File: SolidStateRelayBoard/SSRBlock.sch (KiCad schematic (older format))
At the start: 8 parts, among them Q201 MMBT2222ALT1G, U201 SSR

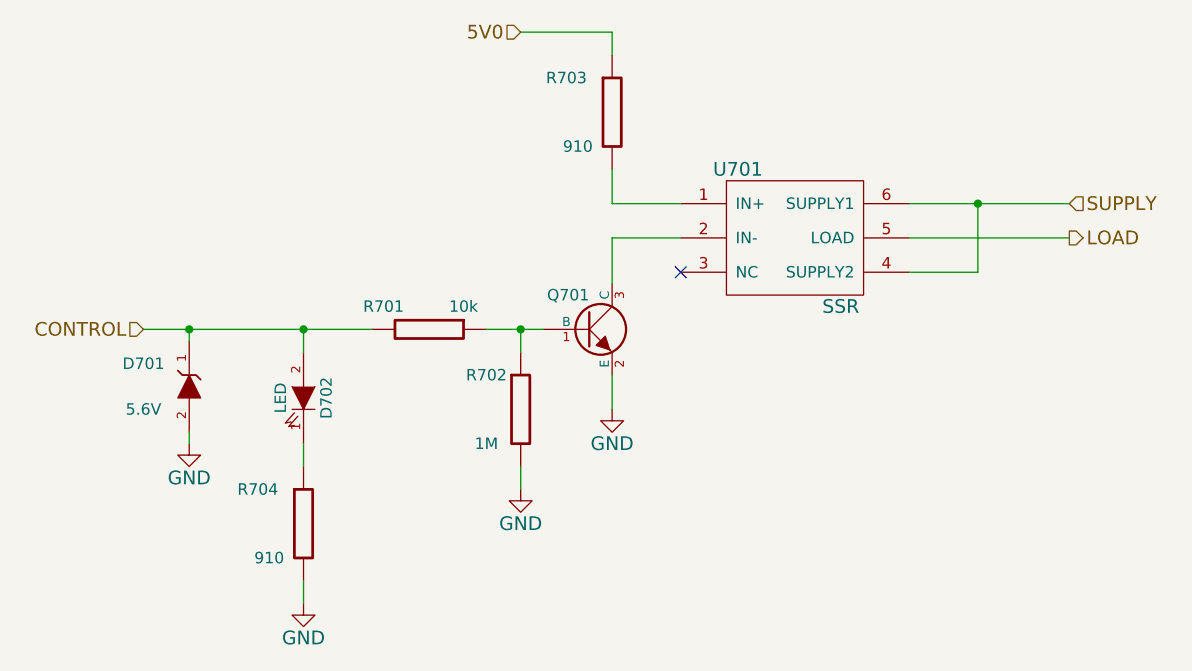
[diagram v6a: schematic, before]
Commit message: Big Changes to SSR
Made a footprint for the XTR and the transistor. Made XTR circuit and
made connected to that it will interface with the mpye’s
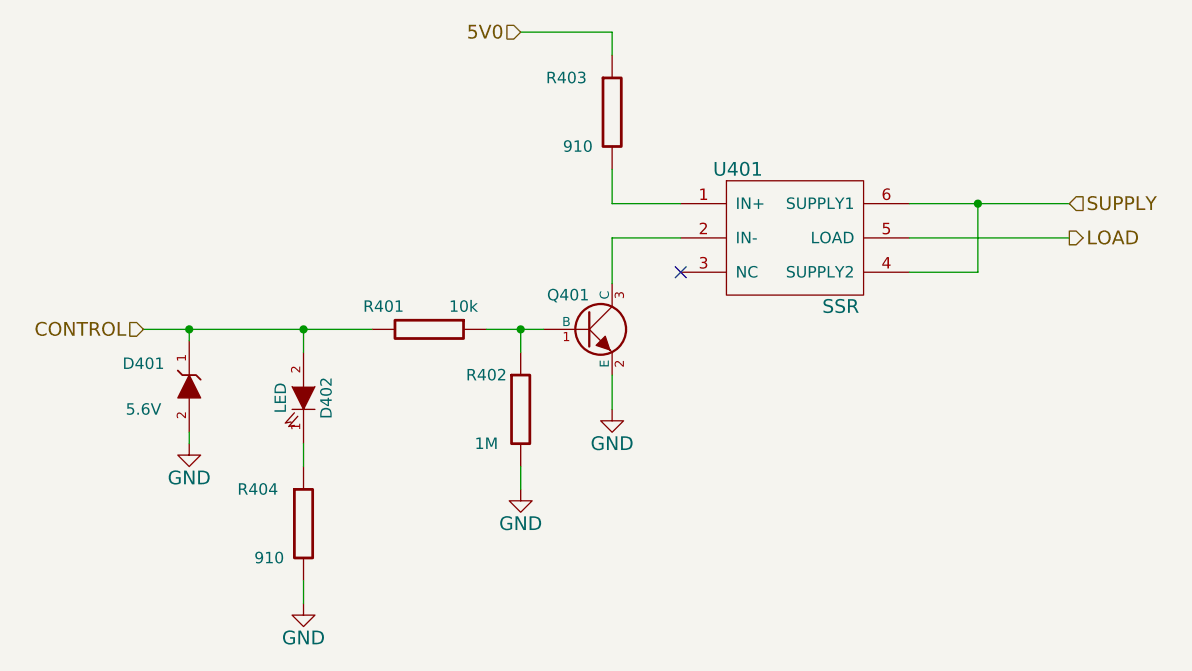
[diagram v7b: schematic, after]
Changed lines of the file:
@@
 $Descr A4 11693 8268
 encoding utf-8
-Sheet 7 14
+Sheet 4 14
 Title ""
 Date ""
@@
 AR Path="/586B7988/586B33BB" Ref="Q1601"  Part="1"
 AR Path="/586B7996/586B33BB" Ref="Q1701"  Part="1"
-F 0 "Q701" H 5100 3400 50  0000 R CNN
+F 0 "Q401" H 5100 3400 50  0000 R CNN
 F 1 "MMBT2222ALT1G" H 5100 3400 50  0001 R CNN
 F 2 "TO_SOT_Packages_SMD:SOT-23_Handsoldering" H 5100 3250 60  0001 C CNN
@@
 AR Path="/586B7988/586B33E9" Ref="R1603"  Part="1"
 AR Path="/586B7996/586B33E9" Ref="R1703"  Part="1"
-F 0 "R703" H 5000 2450 50  0000 C CNN
+F 0 "R403" H 5000 2450 50  0000 C CNN
 F 1 "910" H 5050 2150 50  0000 C CNN
 F 2 "Resistors_SMD:R_1206_HandSoldering" V 5130 2300 30  0001 C CNN
@@
 AR Path="/586B7988/586B3431" Ref="R1601"  Part="1"
 AR Path="/586B7996/586B3431" Ref="R1701"  Part="1"
-F 0 "R701" V 4300 3050 50  0000 C CNN
+F 0 "R401" V 4300 3050 50  0000 C CNN
 F 1 "10k" V 4300 3400 50  0000 C CNN
 F 2 "Resistors_SMD:R_1206_HandSoldering" V 4330 3250 30  0001 C CNN
@@
 	5200 3450 5200 3600
 $Comp
-L GND #PWR036
+L GND #PWR039
 U 1 1 586B354B
 P 5200 3600
-AR Path="/586B2B8E/586B354B" Ref="#PWR036"  Part="1"
-AR Path="/586B3F68/586B354B" Ref="#PWR040"  Part="1"
-AR Path="/586B4A2A/586B354B" Ref="#PWR044"  Part="1"
-AR Path="/586B4A38/586B354B" Ref="#PWR048"  Part="1"
-AR Path="/586B65A6/586B354B" Ref="#PWR052"  Part="1"
-AR Path="/586B65B4/586B354B" Ref="#PWR056"  Part="1"
-AR Path="/586B65C2/586B354B" Ref="#PWR060"  Part="1"
-AR Path="/586B65D0/586B354B" Ref="#PWR064"  Part="1"
-AR Path="/586B7934/586B354B" Ref="#PWR068"  Part="1"
-AR Path="/586B7942/586B354B" Ref="#PWR072"  Part="1"
-AR Path="/586B7950/586B354B" Ref="#PWR076"  Part="1"
-AR Path="/586B795E/586B354B" Ref="#PWR080"  Part="1"
-AR Path="/586B796C/586B354B" Ref="#PWR084"  Part="1"
+AR Path="/586B2B8E/586B354B" Ref="#PWR039"  Part="1"
+AR Path="/586B3F68/586B354B" Ref="#PWR043"  Part="1"
+AR Path="/586B4A2A/586B354B" Ref="#PWR047"  Part="1"
+AR Path="/586B4A38/586B354B" Ref="#PWR051"  Part="1"
+AR Path="/586B65A6/586B354B" Ref="#PWR055"  Part="1"
+AR Path="/586B65B4/586B354B" Ref="#PWR059"  Part="1"
+AR Path="/586B65C2/586B354B" Ref="#PWR063"  Part="1"
+AR Path="/586B65D0/586B354B" Ref="#PWR067"  Part="1"
+AR Path="/586B7934/586B354B" Ref="#PWR071"  Part="1"
+AR Path="/586B7942/586B354B" Ref="#PWR075"  Part="1"
+AR Path="/586B7950/586B354B" Ref="#PWR079"  Part="1"
+AR Path="/586B795E/586B354B" Ref="#PWR083"  Part="1"
+AR Path="/586B796C/586B354B" Ref="#PWR087"  Part="1"
 AR Path="/586B797A/586B354B" Ref="#PWR087"  Part="1"
 AR Path="/586B7988/586B354B" Ref="#PWR091"  Part="1"
 AR Path="/586B7996/586B354B" Ref="#PWR095"  Part="1"
-F 0 "#PWR056" H 5200 3350 60  0001 C CNN
+F 0 "#PWR087" H 5200 3350 60  0001 C CNN
 F 1 "GND" H 5200 3450 60  0000 C CNN
 F 2 "" H 5200 3600 60  0000 C CNN
@@
 AR Path="/586B7988/586B3681" Ref="D1601"  Part="1"
 AR Path="/586B7996/586B3681" Ref="D1701"  Part="1"
-F 0 "D701" V 3450 3700 50  0000 C CNN
+F 0 "D401" V 3450 3700 50  0000 C CNN
 F 1 "5.6V" V 3250 3700 50  0000 C CNN
 F 2 "hyperCustom:SOD-123" H 3350 3500 60  0001 C CNN
@@
 	3350 3700 3350 3750
 $Comp
-L GND #PWR037
+L GND #PWR040
 U 1 1 586B36D9
 P 3350 3750
-AR Path="/586B2B8E/586B36D9" Ref="#PWR037"  Part="1"
-AR Path="/586B3F68/586B36D9" Ref="#PWR041"  Part="1"
-AR Path="/586B4A2A/586B36D9" Ref="#PWR045"  Part="1"
-AR Path="/586B4A38/586B36D9" Ref="#PWR049"  Part="1"
-AR Path="/586B65A6/586B36D9" Ref="#PWR053"  Part="1"
-AR Path="/586B65B4/586B36D9" Ref="#PWR057"  Part="1"
-AR Path="/586B65C2/586B36D9" Ref="#PWR061"  Part="1"
-AR Path="/586B65D0/586B36D9" Ref="#PWR065"  Part="1"
-AR Path="/586B7934/586B36D9" Ref="#PWR069"  Part="1"
-AR Path="/586B7942/586B36D9" Ref="#PWR073"  Part="1"
-AR Path="/586B7950/586B36D9" Ref="#PWR077"  Part="1"
-AR Path="/586B795E/586B36D9" Ref="#PWR081"  Part="1"
-AR Path="/586B796C/586B36D9" Ref="#PWR085"  Part="1"
+AR Path="/586B2B8E/586B36D9" Ref="#PWR040"  Part="1"
+AR Path="/586B3F68/586B36D9" Ref="#PWR044"  Part="1"
+AR Path="/586B4A2A/586B36D9" Ref="#PWR048"  Part="1"
+AR Path="/586B4A38/586B36D9" Ref="#PWR052"  Part="1"
+AR Path="/586B65A6/586B36D9" Ref="#PWR056"  Part="1"
+AR Path="/586B65B4/586B36D9" Ref="#PWR060"  Part="1"
+AR Path="/586B65C2/586B36D9" Ref="#PWR064"  Part="1"
+AR Path="/586B65D0/586B36D9" Ref="#PWR068"  Part="1"
+AR Path="/586B7934/586B36D9" Ref="#PWR072"  Part="1"
+AR Path="/586B7942/586B36D9" Ref="#PWR076"  Part="1"
+AR Path="/586B7950/586B36D9" Ref="#PWR080"  Part="1"
+AR Path="/586B795E/586B36D9" Ref="#PWR084"  Part="1"
+AR Path="/586B796C/586B36D9" Ref="#PWR088"  Part="1"
 AR Path="/586B797A/586B36D9" Ref="#PWR088"  Part="1"
 AR Path="/586B7988/586B36D9" Ref="#PWR092"  Part="1"
 AR Path="/586B7996/586B36D9" Ref="#PWR096"  Part="1"
-F 0 "#PWR057" H 3350 3500 60  0001 C CNN
+F 0 "#PWR088" H 3350 3500 60  0001 C CNN
 F 1 "GND" H 3350 3600 60  0000 C CNN
 F 2 "" H 3350 3750 60  0000 C CNN
@@
 AR Path="/586B7988/586B39A4" Ref="R1602"  Part="1"
 AR Path="/586B7996/586B39A4" Ref="R1702"  Part="1"
-F 0 "R702" H 4650 3750 50  0000 C CNN
+F 0 "R402" H 4650 3750 50  0000 C CNN
 F 1 "1M" H 4650 3450 50  0000 C CNN
 F 2 "Resistors_SMD:R_1206_HandSoldering" V 4730 3600 30  0001 C CNN
@@
 	4800 3850 4800 3950
 $Comp
-L GND #PWR038
+L GND #PWR041
 U 1 1 586B3A19
 P 4800 3950
-AR Path="/586B2B8E/586B3A19" Ref="#PWR038"  Part="1"
-AR Path="/586B3F68/586B3A19" Ref="#PWR042"  Part="1"
-AR Path="/586B4A2A/586B3A19" Ref="#PWR046"  Part="1"
-AR Path="/586B4A38/586B3A19" Ref="#PWR050"  Part="1"
-AR Path="/586B65A6/586B3A19" Ref="#PWR054"  Part="1"
-AR Path="/586B65B4/586B3A19" Ref="#PWR058"  Part="1"
-AR Path="/586B65C2/586B3A19" Ref="#PWR062"  Part="1"
-AR Path="/586B65D0/586B3A19" Ref="#PWR066"  Part="1"
-AR Path="/586B7934/586B3A19" Ref="#PWR070"  Part="1"
-AR Path="/586B7942/586B3A19" Ref="#PWR074"  Part="1"
-AR Path="/586B7950/586B3A19" Ref="#PWR078"  Part="1"
-AR Path="/586B795E/586B3A19" Ref="#PWR082"  Part="1"
-AR Path="/586B796C/586B3A19" Ref="#PWR086"  Part="1"
+AR Path="/586B2B8E/586B3A19" Ref="#PWR041"  Part="1"
+AR Path="/586B3F68/586B3A19" Ref="#PWR045"  Part="1"
+AR Path="/586B4A2A/586B3A19" Ref="#PWR049"  Part="1"
+AR Path="/586B4A38/586B3A19" Ref="#PWR053"  Part="1"
+AR Path="/586B65A6/586B3A19" Ref="#PWR057"  Part="1"
+AR Path="/586B65B4/586B3A19" Ref="#PWR061"  Part="1"
+AR Path="/586B65C2/586B3A19" Ref="#PWR065"  Part="1"
+AR Path="/586B65D0/586B3A19" Ref="#PWR069"  Part="1"
+AR Path="/586B7934/586B3A19" Ref="#PWR073"  Part="1"
+AR Path="/586B7942/586B3A19" Ref="#PWR077"  Part="1"
+AR Path="/586B7950/586B3A19" Ref="#PWR081"  Part="1"
+AR Path="/586B795E/586B3A19" Ref="#PWR085"  Part="1"
+AR Path="/586B796C/586B3A19" Ref="#PWR089"  Part="1"
 AR Path="/586B797A/586B3A19" Ref="#PWR089"  Part="1"
 AR Path="/586B7988/586B3A19" Ref="#PWR093"  Part="1"
 AR Path="/586B7996/586B3A19" Ref="#PWR097"  Part="1"
-F 0 "#PWR058" H 4800 3700 60  0001 C CNN
+F 0 "#PWR089" H 4800 3700 60  0001 C CNN
 F 1 "GND" H 4800 3800 60  0000 C CNN
 F 2 "" H 4800 3950 60  0000 C CNN
@@
 AR Path="/586B7988/586D88E1" Ref="U1601"  Part="1"
 AR Path="/586B7996/586D88E1" Ref="U1701"  Part="1"
-F 0 "U701" H 5750 3150 60  0000 C CNN
+F 0 "U401" H 5750 3150 60  0000 C CNN
 F 1 "SSR" H 6200 2550 60  0000 C CNN
 F 2 "hyperCustom:VISHAY_6SMD_OPTOCOUPLER" H 6000 2850 60  0001 C CNN
@@
 AR Path="/586B7996/586E6B18" Ref="D1702"  Part="1"
 AR Path="/586E6B18" Ref="D202"  Part="1"
-F 0 "D702" H 3850 3650 50  0000 C CNN
+F 0 "D402" H 3850 3650 50  0000 C CNN
 F 1 "LED" H 3850 3450 50  0000 C CNN
 F 2 "hyperCustom:SOD-123" H 3850 3550 60  0001 C CNN
@@
 AR Path="/586B7988/586E6B5D" Ref="R1604"  Part="1"
 AR Path="/586B7996/586E6B5D" Ref="R1704"  Part="1"
-F 0 "R704" H 3650 4250 50  0000 C CNN
+F 0 "R404" H 3650 4250 50  0000 C CNN
 F 1 "910" H 3700 3950 50  0000 C CNN
 F 2 "Resistors_SMD:R_1206_HandSoldering" V 3780 4100 30  0001 C CNN
@@
 	3850 4350 3850 4450
 $Comp
-L GND #PWR039
+L GND #PWR042
 U 1 1 586E6C2B
 P 3850 4450
-AR Path="/586B2B8E/586E6C2B" Ref="#PWR039"  Part="1"
-AR Path="/586B3F68/586E6C2B" Ref="#PWR043"  Part="1"
-AR Path="/586B4A2A/586E6C2B" Ref="#PWR047"  Part="1"
-AR Path="/586B4A38/586E6C2B" Ref="#PWR051"  Part="1"
-AR Path="/586B65A6/586E6C2B" Ref="#PWR055"  Part="1"
-AR Path="/586B65B4/586E6C2B" Ref="#PWR059"  Part="1"
-AR Path="/586B65C2/586E6C2B" Ref="#PWR063"  Part="1"
-AR Path="/586B65D0/586E6C2B" Ref="#PWR067"  Part="1"
-AR Path="/586B7934/586E6C2B" Ref="#PWR071"  Part="1"
-AR Path="/586B7942/586E6C2B" Ref="#PWR075"  Part="1"
-AR Path="/586B7950/586E6C2B" Ref="#PWR079"  Part="1"
-AR Path="/586B795E/586E6C2B" Ref="#PWR083"  Part="1"
-AR Path="/586B796C/586E6C2B" Ref="#PWR087"  Part="1"
+AR Path="/586B2B8E/586E6C2B" Ref="#PWR042"  Part="1"
+AR Path="/586B3F68/586E6C2B" Ref="#PWR046"  Part="1"
+AR Path="/586B4A2A/586E6C2B" Ref="#PWR050"  Part="1"
+AR Path="/586B4A38/586E6C2B" Ref="#PWR054"  Part="1"
+AR Path="/586B65A6/586E6C2B" Ref="#PWR058"  Part="1"
+AR Path="/586B65B4/586E6C2B" Ref="#PWR062"  Part="1"
+AR Path="/586B65C2/586E6C2B" Ref="#PWR066"  Part="1"
+AR Path="/586B65D0/586E6C2B" Ref="#PWR070"  Part="1"
+AR Path="/586B7934/586E6C2B" Ref="#PWR074"  Part="1"
+AR Path="/586B7942/586E6C2B" Ref="#PWR078"  Part="1"
+AR Path="/586B7950/586E6C2B" Ref="#PWR082"  Part="1"
+AR Path="/586B795E/586E6C2B" Ref="#PWR086"  Part="1"
+AR Path="/586B796C/586E6C2B" Ref="#PWR090"  Part="1"
 AR Path="/586B797A/586E6C2B" Ref="#PWR090"  Part="1"
 AR Path="/586B7988/586E6C2B" Ref="#PWR094"  Part="1"
 AR Path="/586B7996/586E6C2B" Ref="#PWR098"  Part="1"
-F 0 "#PWR059" H 3850 4200 60  0001 C CNN
+F 0 "#PWR090" H 3850 4200 60  0001 C CNN
 F 1 "GND" H 3850 4300 60  0000 C CNN
 F 2 "" H 3850 4450 60  0000 C CNN

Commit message: SSR Board
Small changes to PCB
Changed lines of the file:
@@
 $Descr A4 11693 8268
 encoding utf-8
-Sheet 4 14
+Sheet 2 14
 Title ""
 Date ""
@@
 AR Path="/586B7988/586B33BB" Ref="Q1601"  Part="1"
 AR Path="/586B7996/586B33BB" Ref="Q1701"  Part="1"
-F 0 "Q401" H 5100 3400 50  0000 R CNN
+F 0 "Q201" H 5100 3400 50  0000 R CNN
 F 1 "MMBT2222ALT1G" H 5100 3400 50  0001 R CNN
 F 2 "TO_SOT_Packages_SMD:SOT-23_Handsoldering" H 5100 3250 60  0001 C CNN
@@
 AR Path="/586B7988/586B33E9" Ref="R1603"  Part="1"
 AR Path="/586B7996/586B33E9" Ref="R1703"  Part="1"
-F 0 "R403" H 5000 2450 50  0000 C CNN
+F 0 "R203" H 5000 2450 50  0000 C CNN
 F 1 "910" H 5050 2150 50  0000 C CNN
 F 2 "Resistors_SMD:R_1206_HandSoldering" V 5130 2300 30  0001 C CNN
@@
 AR Path="/586B7988/586B3431" Ref="R1601"  Part="1"
 AR Path="/586B7996/586B3431" Ref="R1701"  Part="1"
-F 0 "R401" V 4300 3050 50  0000 C CNN
+F 0 "R201" V 4300 3050 50  0000 C CNN
 F 1 "10k" V 4300 3400 50  0000 C CNN
 F 2 "Resistors_SMD:R_1206_HandSoldering" V 4330 3250 30  0001 C CNN
@@
 	5200 3450 5200 3600
 $Comp
-L GND #PWR039
+L GND #PWR033
 U 1 1 586B354B
 P 5200 3600
-AR Path="/586B2B8E/586B354B" Ref="#PWR039"  Part="1"
-AR Path="/586B3F68/586B354B" Ref="#PWR043"  Part="1"
-AR Path="/586B4A2A/586B354B" Ref="#PWR047"  Part="1"
-AR Path="/586B4A38/586B354B" Ref="#PWR051"  Part="1"
-AR Path="/586B65A6/586B354B" Ref="#PWR055"  Part="1"
-AR Path="/586B65B4/586B354B" Ref="#PWR059"  Part="1"
-AR Path="/586B65C2/586B354B" Ref="#PWR063"  Part="1"
-AR Path="/586B65D0/586B354B" Ref="#PWR067"  Part="1"
-AR Path="/586B7934/586B354B" Ref="#PWR071"  Part="1"
-AR Path="/586B7942/586B354B" Ref="#PWR075"  Part="1"
-AR Path="/586B7950/586B354B" Ref="#PWR079"  Part="1"
-AR Path="/586B795E/586B354B" Ref="#PWR083"  Part="1"
-AR Path="/586B796C/586B354B" Ref="#PWR087"  Part="1"
+AR Path="/586B2B8E/586B354B" Ref="#PWR033"  Part="1"
+AR Path="/586B3F68/586B354B" Ref="#PWR037"  Part="1"
+AR Path="/586B4A2A/586B354B" Ref="#PWR041"  Part="1"
+AR Path="/586B4A38/586B354B" Ref="#PWR045"  Part="1"
+AR Path="/586B65A6/586B354B" Ref="#PWR049"  Part="1"
+AR Path="/586B65B4/586B354B" Ref="#PWR053"  Part="1"
+AR Path="/586B65C2/586B354B" Ref="#PWR057"  Part="1"
+AR Path="/586B65D0/586B354B" Ref="#PWR061"  Part="1"
+AR Path="/586B7934/586B354B" Ref="#PWR065"  Part="1"
+AR Path="/586B7942/586B354B" Ref="#PWR069"  Part="1"
+AR Path="/586B7950/586B354B" Ref="#PWR073"  Part="1"
+AR Path="/586B795E/586B354B" Ref="#PWR077"  Part="1"
+AR Path="/586B796C/586B354B" Ref="#PWR081"  Part="1"
 AR Path="/586B797A/586B354B" Ref="#PWR087"  Part="1"
 AR Path="/586B7988/586B354B" Ref="#PWR091"  Part="1"
 AR Path="/586B7996/586B354B" Ref="#PWR095"  Part="1"
-F 0 "#PWR087" H 5200 3350 60  0001 C CNN
+F 0 "#PWR033" H 5200 3350 60  0001 C CNN
 F 1 "GND" H 5200 3450 60  0000 C CNN
 F 2 "" H 5200 3600 60  0000 C CNN
@@
 AR Path="/586B7988/586B3681" Ref="D1601"  Part="1"
 AR Path="/586B7996/586B3681" Ref="D1701"  Part="1"
-F 0 "D401" V 3450 3700 50  0000 C CNN
+F 0 "D201" V 3450 3700 50  0000 C CNN
 F 1 "5.6V" V 3250 3700 50  0000 C CNN
 F 2 "hyperCustom:SOD-123" H 3350 3500 60  0001 C CNN
@@
 	3350 3700 3350 3750
 $Comp
-L GND #PWR040
+L GND #PWR034
 U 1 1 586B36D9
 P 3350 3750
-AR Path="/586B2B8E/586B36D9" Ref="#PWR040"  Part="1"
-AR Path="/586B3F68/586B36D9" Ref="#PWR044"  Part="1"
-AR Path="/586B4A2A/586B36D9" Ref="#PWR048"  Part="1"
-AR Path="/586B4A38/586B36D9" Ref="#PWR052"  Part="1"
-AR Path="/586B65A6/586B36D9" Ref="#PWR056"  Part="1"
-AR Path="/586B65B4/586B36D9" Ref="#PWR060"  Part="1"
-AR Path="/586B65C2/586B36D9" Ref="#PWR064"  Part="1"
-AR Path="/586B65D0/586B36D9" Ref="#PWR068"  Part="1"
-AR Path="/586B7934/586B36D9" Ref="#PWR072"  Part="1"
-AR Path="/586B7942/586B36D9" Ref="#PWR076"  Part="1"
-AR Path="/586B7950/586B36D9" Ref="#PWR080"  Part="1"
-AR Path="/586B795E/586B36D9" Ref="#PWR084"  Part="1"
-AR Path="/586B796C/586B36D9" Ref="#PWR088"  Part="1"
+AR Path="/586B2B8E/586B36D9" Ref="#PWR034"  Part="1"
+AR Path="/586B3F68/586B36D9" Ref="#PWR038"  Part="1"
+AR Path="/586B4A2A/586B36D9" Ref="#PWR042"  Part="1"
+AR Path="/586B4A38/586B36D9" Ref="#PWR046"  Part="1"
+AR Path="/586B65A6/586B36D9" Ref="#PWR050"  Part="1"
+AR Path="/586B65B4/586B36D9" Ref="#PWR054"  Part="1"
+AR Path="/586B65C2/586B36D9" Ref="#PWR058"  Part="1"
+AR Path="/586B65D0/586B36D9" Ref="#PWR062"  Part="1"
+AR Path="/586B7934/586B36D9" Ref="#PWR066"  Part="1"
+AR Path="/586B7942/586B36D9" Ref="#PWR070"  Part="1"
+AR Path="/586B7950/586B36D9" Ref="#PWR074"  Part="1"
+AR Path="/586B795E/586B36D9" Ref="#PWR078"  Part="1"
+AR Path="/586B796C/586B36D9" Ref="#PWR082"  Part="1"
 AR Path="/586B797A/586B36D9" Ref="#PWR088"  Part="1"
 AR Path="/586B7988/586B36D9" Ref="#PWR092"  Part="1"
 AR Path="/586B7996/586B36D9" Ref="#PWR096"  Part="1"
-F 0 "#PWR088" H 3350 3500 60  0001 C CNN
+F 0 "#PWR034" H 3350 3500 60  0001 C CNN
 F 1 "GND" H 3350 3600 60  0000 C CNN
 F 2 "" H 3350 3750 60  0000 C CNN
@@
 AR Path="/586B7988/586B39A4" Ref="R1602"  Part="1"
 AR Path="/586B7996/586B39A4" Ref="R1702"  Part="1"
-F 0 "R402" H 4650 3750 50  0000 C CNN
+F 0 "R202" H 4650 3750 50  0000 C CNN
 F 1 "1M" H 4650 3450 50  0000 C CNN
 F 2 "Resistors_SMD:R_1206_HandSoldering" V 4730 3600 30  0001 C CNN
@@
 	4800 3850 4800 3950
 $Comp
-L GND #PWR041
+L GND #PWR035
 U 1 1 586B3A19
 P 4800 3950
-AR Path="/586B2B8E/586B3A19" Ref="#PWR041"  Part="1"
-AR Path="/586B3F68/586B3A19" Ref="#PWR045"  Part="1"
-AR Path="/586B4A2A/586B3A19" Ref="#PWR049"  Part="1"
-AR Path="/586B4A38/586B3A19" Ref="#PWR053"  Part="1"
-AR Path="/586B65A6/586B3A19" Ref="#PWR057"  Part="1"
-AR Path="/586B65B4/586B3A19" Ref="#PWR061"  Part="1"
-AR Path="/586B65C2/586B3A19" Ref="#PWR065"  Part="1"
-AR Path="/586B65D0/586B3A19" Ref="#PWR069"  Part="1"
-AR Path="/586B7934/586B3A19" Ref="#PWR073"  Part="1"
-AR Path="/586B7942/586B3A19" Ref="#PWR077"  Part="1"
-AR Path="/586B7950/586B3A19" Ref="#PWR081"  Part="1"
-AR Path="/586B795E/586B3A19" Ref="#PWR085"  Part="1"
-AR Path="/586B796C/586B3A19" Ref="#PWR089"  Part="1"
+AR Path="/586B2B8E/586B3A19" Ref="#PWR035"  Part="1"
+AR Path="/586B3F68/586B3A19" Ref="#PWR039"  Part="1"
+AR Path="/586B4A2A/586B3A19" Ref="#PWR043"  Part="1"
+AR Path="/586B4A38/586B3A19" Ref="#PWR047"  Part="1"
+AR Path="/586B65A6/586B3A19" Ref="#PWR051"  Part="1"
+AR Path="/586B65B4/586B3A19" Ref="#PWR055"  Part="1"
+AR Path="/586B65C2/586B3A19" Ref="#PWR059"  Part="1"
+AR Path="/586B65D0/586B3A19" Ref="#PWR063"  Part="1"
+AR Path="/586B7934/586B3A19" Ref="#PWR067"  Part="1"
+AR Path="/586B7942/586B3A19" Ref="#PWR071"  Part="1"
+AR Path="/586B7950/586B3A19" Ref="#PWR075"  Part="1"
+AR Path="/586B795E/586B3A19" Ref="#PWR079"  Part="1"
+AR Path="/586B796C/586B3A19" Ref="#PWR083"  Part="1"
 AR Path="/586B797A/586B3A19" Ref="#PWR089"  Part="1"
 AR Path="/586B7988/586B3A19" Ref="#PWR093"  Part="1"
 AR Path="/586B7996/586B3A19" Ref="#PWR097"  Part="1"
-F 0 "#PWR089" H 4800 3700 60  0001 C CNN
+F 0 "#PWR035" H 4800 3700 60  0001 C CNN
 F 1 "GND" H 4800 3800 60  0000 C CNN
 F 2 "" H 4800 3950 60  0000 C CNN
@@
 AR Path="/586B7988/586D88E1" Ref="U1601"  Part="1"
 AR Path="/586B7996/586D88E1" Ref="U1701"  Part="1"
-F 0 "U401" H 5750 3150 60  0000 C CNN
+F 0 "U201" H 5750 3150 60  0000 C CNN
 F 1 "SSR" H 6200 2550 60  0000 C CNN
 F 2 "hyperCustom:VISHAY_6SMD_OPTOCOUPLER" H 6000 2850 60  0001 C CNN
@@
 AR Path="/586B7996/586E6B18" Ref="D1702"  Part="1"
 AR Path="/586E6B18" Ref="D202"  Part="1"
-F 0 "D402" H 3850 3650 50  0000 C CNN
+F 0 "D202" H 3850 3650 50  0000 C CNN
 F 1 "LED" H 3850 3450 50  0000 C CNN
 F 2 "hyperCustom:SOD-123" H 3850 3550 60  0001 C CNN
@@
 AR Path="/586B7988/586E6B5D" Ref="R1604"  Part="1"
 AR Path="/586B7996/586E6B5D" Ref="R1704"  Part="1"
-F 0 "R404" H 3650 4250 50  0000 C CNN
+F 0 "R204" H 3650 4250 50  0000 C CNN
 F 1 "910" H 3700 3950 50  0000 C CNN
 F 2 "Resistors_SMD:R_1206_HandSoldering" V 3780 4100 30  0001 C CNN
@@
 	3850 4350 3850 4450
 $Comp
-L GND #PWR042
+L GND #PWR036
 U 1 1 586E6C2B
 P 3850 4450
-AR Path="/586B2B8E/586E6C2B" Ref="#PWR042"  Part="1"
-AR Path="/586B3F68/586E6C2B" Ref="#PWR046"  Part="1"
-AR Path="/586B4A2A/586E6C2B" Ref="#PWR050"  Part="1"
-AR Path="/586B4A38/586E6C2B" Ref="#PWR054"  Part="1"
-AR Path="/586B65A6/586E6C2B" Ref="#PWR058"  Part="1"
-AR Path="/586B65B4/586E6C2B" Ref="#PWR062"  Part="1"
-AR Path="/586B65C2/586E6C2B" Ref="#PWR066"  Part="1"
-AR Path="/586B65D0/586E6C2B" Ref="#PWR070"  Part="1"
-AR Path="/586B7934/586E6C2B" Ref="#PWR074"  Part="1"
-AR Path="/586B7942/586E6C2B" Ref="#PWR078"  Part="1"
-AR Path="/586B7950/586E6C2B" Ref="#PWR082"  Part="1"
-AR Path="/586B795E/586E6C2B" Ref="#PWR086"  Part="1"
-AR Path="/586B796C/586E6C2B" Ref="#PWR090"  Part="1"
+AR Path="/586B2B8E/586E6C2B" Ref="#PWR036"  Part="1"
+AR Path="/586B3F68/586E6C2B" Ref="#PWR040"  Part="1"
+AR Path="/586B4A2A/586E6C2B" Ref="#PWR044"  Part="1"
+AR Path="/586B4A38/586E6C2B" Ref="#PWR048"  Part="1"
+AR Path="/586B65A6/586E6C2B" Ref="#PWR052"  Part="1"
+AR Path="/586B65B4/586E6C2B" Ref="#PWR056"  Part="1"
+AR Path="/586B65C2/586E6C2B" Ref="#PWR060"  Part="1"
+AR Path="/586B65D0/586E6C2B" Ref="#PWR064"  Part="1"
+AR Path="/586B7934/586E6C2B" Ref="#PWR068"  Part="1"
+AR Path="/586B7942/586E6C2B" Ref="#PWR072"  Part="1"
+AR Path="/586B7950/586E6C2B" Ref="#PWR076"  Part="1"
+AR Path="/586B795E/586E6C2B" Ref="#PWR080"  Part="1"
+AR Path="/586B796C/586E6C2B" Ref="#PWR084"  Part="1"
 AR Path="/586B797A/586E6C2B" Ref="#PWR090"  Part="1"
 AR Path="/586B7988/586E6C2B" Ref="#PWR094"  Part="1"
 AR Path="/586B7996/586E6C2B" Ref="#PWR098"  Part="1"
-F 0 "#PWR090" H 3850 4200 60  0001 C CNN
+F 0 "#PWR036" H 3850 4200 60  0001 C CNN
 F 1 "GND" H 3850 4300 60  0000 C CNN
 F 2 "" H 3850 4450 60  0000 C CNN
